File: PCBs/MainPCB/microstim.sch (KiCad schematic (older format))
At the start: 105 parts, among them J1 Conn_02x08_Odd_Even, J2 Conn_Coaxial, J3 Conn_Coaxial, J6 Screw_Terminal_01x02, J7 Conn_Coaxial, J8 Screw_Terminal_01x02, J9 Conn_Coaxial, SW1 SW_Push, U1 Teensy3.5, U10 AD8276, U11 INA826, U12 DG509ACWE, U13 CC3-0512DF-E, U14 ISO7760, U15 ISO7341C, U16 L78L05_SO8, U17 AD5752, U18 AD7321, U19 AD1582, U2 CC3-0512DF-E, U20 OPA197, U21 AD8276, U22 INA826, U23 DG509ACWE, U3 ISO7760, U4 ISO7341C, U5 L78L05_SO8, U6 AD5752, U7 AD7321, U8 AD1582, U9 OPA197

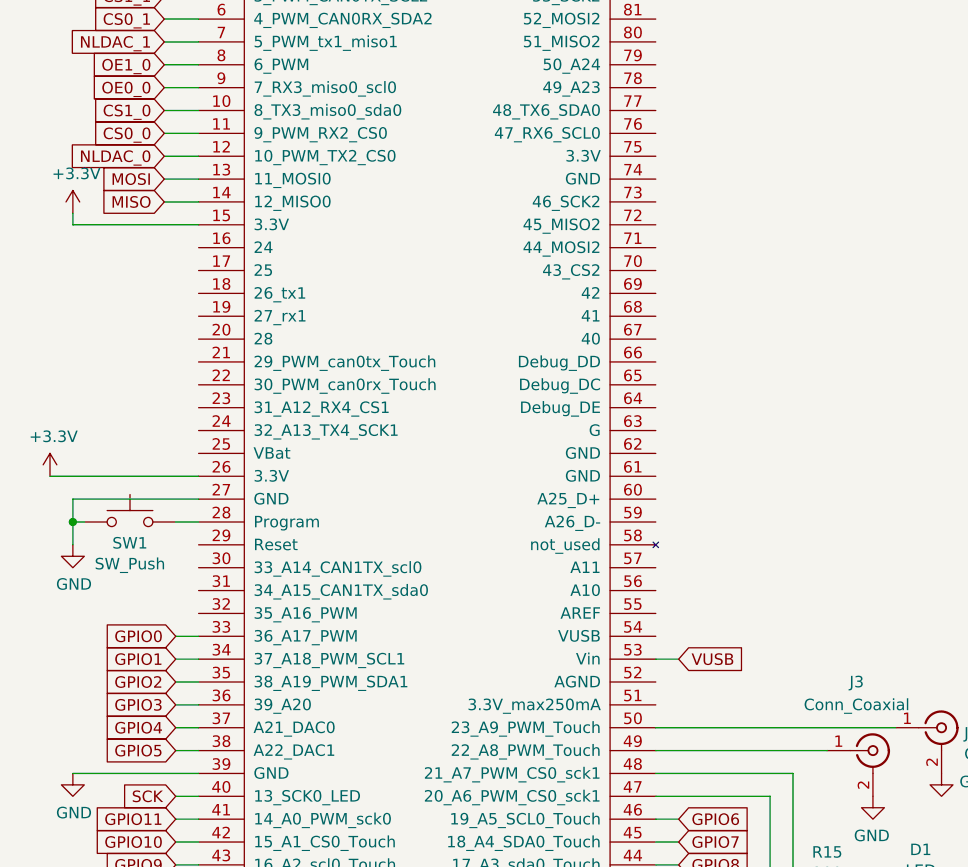
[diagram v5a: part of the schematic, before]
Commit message: merged in benchmarking into v3b. changed 3.3v power pin so that design is compatible with teensy 3.1/2 and 3.5/6.
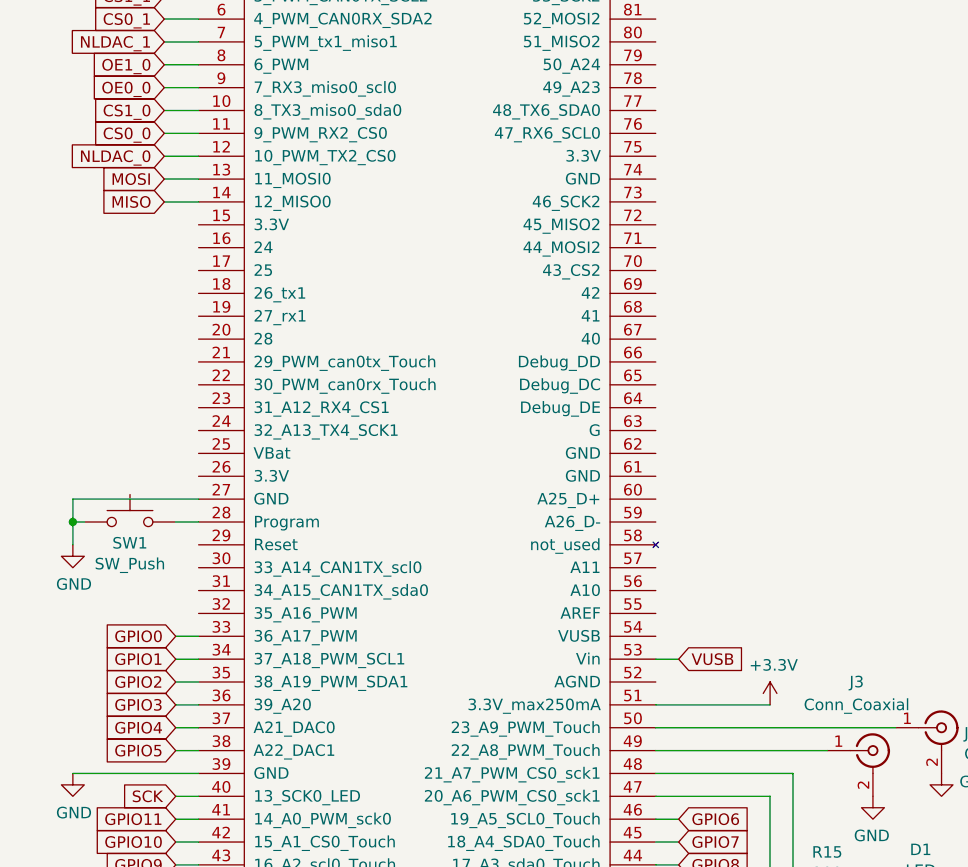
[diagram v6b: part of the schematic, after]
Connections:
- net +3V3: now also U1.51 (3.3V_max250mA); no longer U1.15 (3.3V), U1.26 (3.3V)
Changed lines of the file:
@@
 	6050 1850 5850 1850
 $Comp
-L power:+3.3V #PWR03
-U 1 1 5B7D2A4B
-P 700 1850
-F 0 "#PWR03" H 700 1700 50  0001 C CNN
-F 1 "+3.3V" H 715 2023 50  0000 C CNN
-F 2 "" H 700 1850 50  0001 C CNN
-F 3 "" H 700 1850 50  0001 C CNN
-	1    700  1850
-	1    0    0    -1
-$EndComp
-$Comp
 L Device:R_US R5
 U 1 1 5B7EBBC6
@@
 Text GLabel 1100 1500 0    50   Input ~ 0
 CS0_0
-Wire Wire Line
-	1250 1900 700  1900
-Wire Wire Line
-	700  1900 700  1850
 Text GLabel 8300 2450 0    50   Input ~ 0
 SCK_0i
@@
 Wire Wire Line
 	700  3200 700  3300
-Wire Wire Line
-	600  3000 1250 3000
 Text GLabel 2600 5200 2    50   Input ~ 0
 VUSB
@@
 Wire Wire Line
 	2600 5200 2500 5200
-$Comp
-L power:+3.3V #PWR0111
-U 1 1 5D1270A2
-P 600 3000
-F 0 "#PWR0111" H 600 2850 50  0001 C CNN
-F 1 "+3.3V" H 615 3173 50  0000 C CNN
-F 2 "" H 600 3000 50  0001 C CNN
-F 3 "" H 600 3000 50  0001 C CNN
-	1    600  3000
-	1    0    0    -1
-$EndComp
 Text GLabel 2600 5900 2    50   Input ~ 0
 GPIO11
@@
 Text Notes 5200 2700 1    79   ~ 0
 Stim channel 0
+$Comp
+L power:+3.3V #PWR0115
+U 1 1 5C672D77
+P 3750 4000
+F 0 "#PWR0115" H 3750 3850 50  0001 C CNN
+F 1 "+3.3V" H 3765 4173 50  0000 C CNN
+F 2 "" H 3750 4000 50  0001 C CNN
+F 3 "" H 3750 4000 50  0001 C CNN
+	1    3750 4000
+	1    0    0    -1
+$EndComp
+Wire Wire Line
+	3250 4000 3750 4000
 $EndSCHEMATC

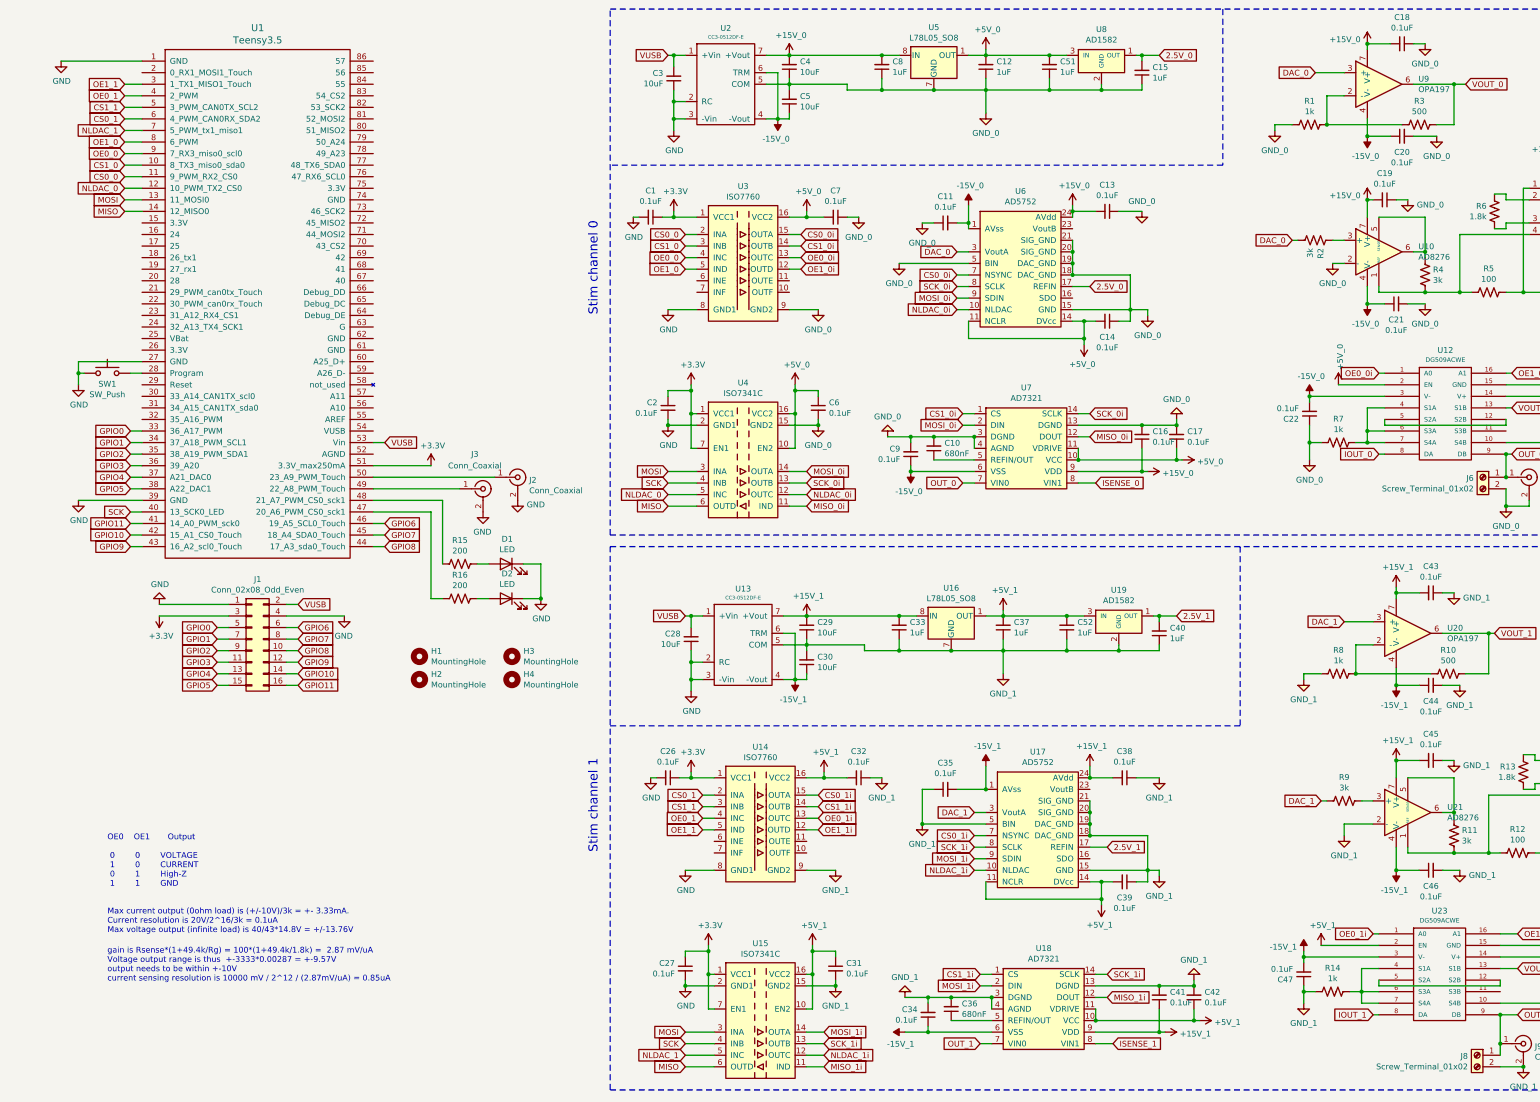
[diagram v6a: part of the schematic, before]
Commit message: boatload of updates via jons suggestions. de-isolated grounds via large resistors+capacitors (to prevent static buildup on animal or issues with large discharges). increased resistor values in voltage output non-inverting amplifier.
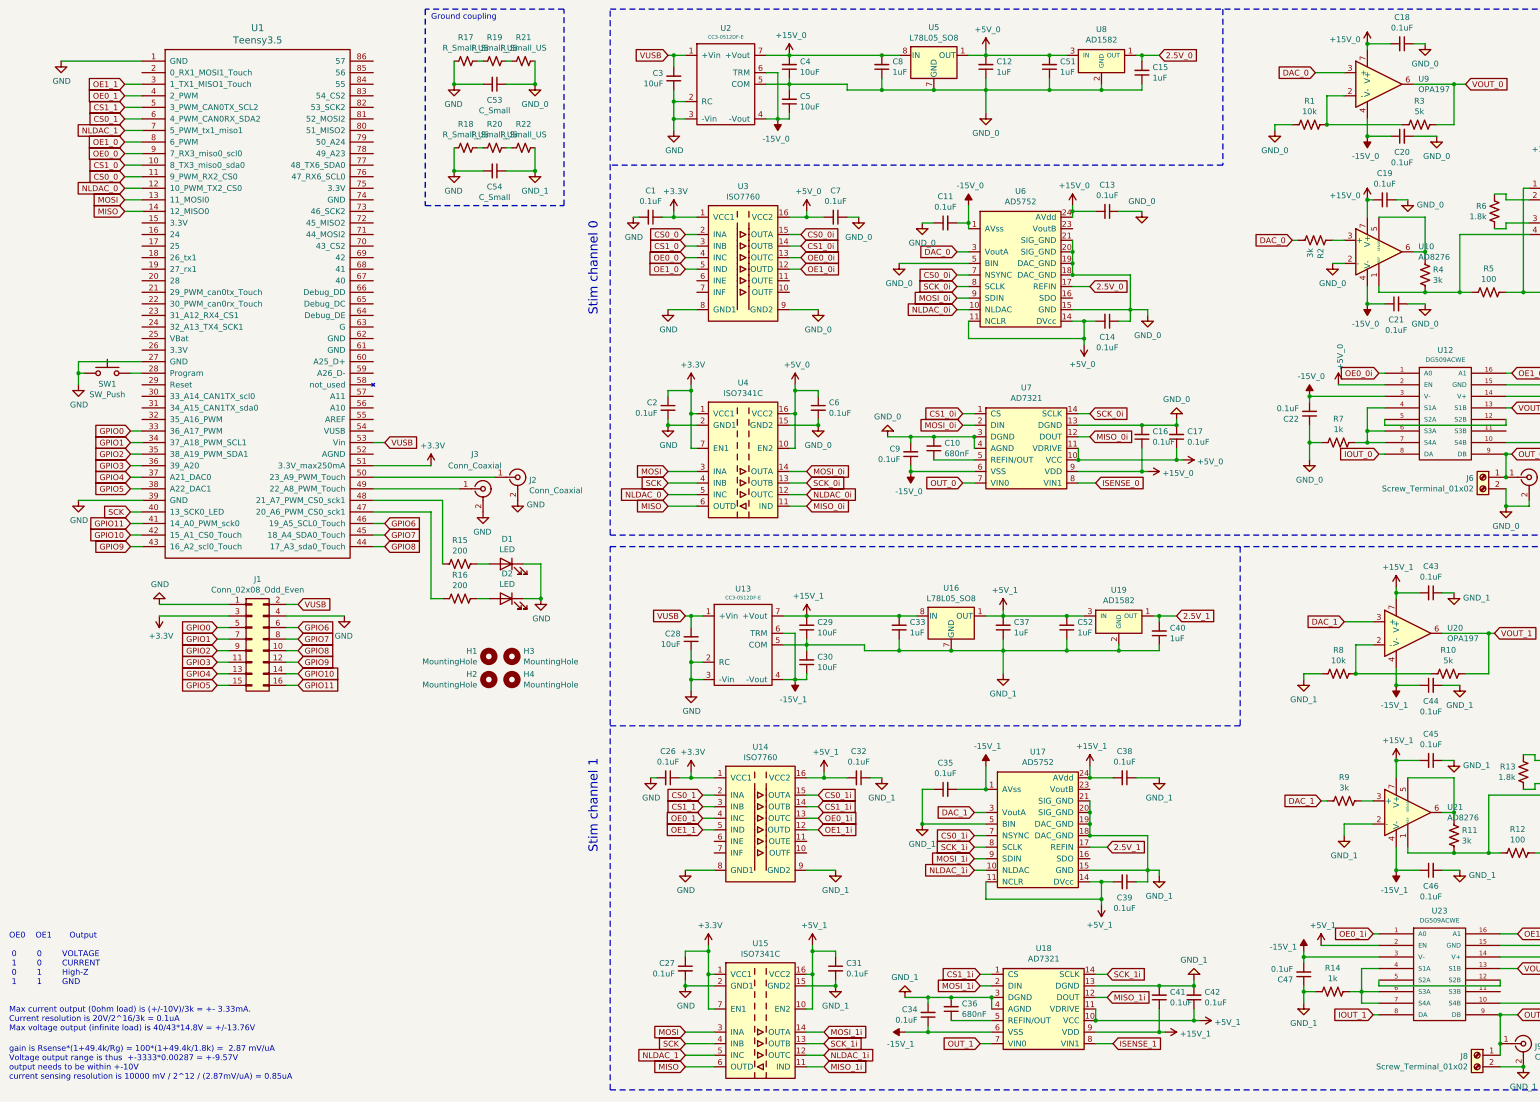
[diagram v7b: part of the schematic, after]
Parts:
- added C53, C54: C_Small, Capacitor_THT:C_Disc_D12.5mm_W5.0mm_P10.00mm, symbol Device:C_Small
- added R17, R18, R19, R20, R21, R22: R_Small_US, Resistor_SMD:R_1210_3225Metric_Pad1.42x2.65mm_HandSolder, symbol Device:R_Small_US
- R1, R8: value 1k -> 10k
- R10, R3: value 500 -> 5k
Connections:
- net GND: now also C53.2, C54.2, R17.2, R18.2
- net GND_0: now also C53.1, R21.1
- net GND_1: now also C54.1, R22.1
- new net: R17.1, R19.2
- new net: R19.1, R21.2
- new net: R18.1, R20.2
- new net: R20.1, R22.2
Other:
- note added: "Ground coupling"
- moved on the sheet: H1, H2
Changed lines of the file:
@@
 Wire Wire Line
 	13050 1700 13250 1700
-Text Notes 950  8550 0    50   ~ 0
+Text Notes 100  9400 0    50   ~ 0
 gain is Rsense*(1+49.4k/Rg) = 100*(1+49.4k/1.8k) =  2.87 mV/uA\nVoltage output range is thus  +-3333*0.00287 = +-9.57V\noutput needs to be within +-10V\ncurrent sensing resolution is 10000 mV / 2^12 / (2.87mV/uA) = 0.85uA\n\n
-Text Notes 950  8050 0    50   ~ 0
+Text Notes 100  8900 0    50   ~ 0
 Max current output (0ohm load) is (+/-10V)/3k = +- 3.33mA.\nCurrent resolution is 20V/2^16/3k = 0.1uA\nMax voltage output (infinite load) is 40/43*14.8V = +/-13.76V
 $Comp
@@
 L Mechanical:MountingHole H1
 U 1 1 5C07145A
-P 3650 5650
-F 0 "H1" H 3750 5696 50  0000 L CNN
-F 1 "MountingHole" H 3750 5605 50  0000 L CNN
-F 2 "MountingHole:MountingHole_4.3mm_M4" H 3650 5650 50  0001 C CNN
-F 3 "~" H 3650 5650 50  0001 C CNN
-	1    3650 5650
+P 4250 5650
+F 0 "H1" H 4150 5696 50  0000 R CNN
+F 1 "MountingHole" H 4150 5605 50  0000 R CNN
+F 2 "MountingHole:MountingHole_4.3mm_M4" H 4250 5650 50  0001 C CNN
+F 3 "~" H 4250 5650 50  0001 C CNN
+	1    4250 5650
 	1    0    0    -1
 $EndComp
@@
 L Mechanical:MountingHole H2
 U 1 1 5C071952
-P 3650 5850
-F 0 "H2" H 3750 5896 50  0000 L CNN
-F 1 "MountingHole" H 3750 5805 50  0000 L CNN
-F 2 "MountingHole:MountingHole_4.3mm_M4" H 3650 5850 50  0001 C CNN
-F 3 "~" H 3650 5850 50  0001 C CNN
-	1    3650 5850
+P 4250 5850
+F 0 "H2" H 4150 5896 50  0000 R CNN
+F 1 "MountingHole" H 4150 5805 50  0000 R CNN
+F 2 "MountingHole:MountingHole_4.3mm_M4" H 4250 5850 50  0001 C CNN
+F 3 "~" H 4250 5850 50  0001 C CNN
+	1    4250 5850
 	1    0    0    -1
 $EndComp
@@
 P 12300 1050
 F 0 "R3" V 12505 1050 50  0000 C CNN
-F 1 "500" V 12414 1050 50  0000 C CNN
+F 1 "5k" V 12414 1050 50  0000 C CNN
 F 2 "Resistor_SMD:R_0603_1608Metric" V 12340 1040 50  0001 C CNN
 F 3 "~" H 12300 1050 50  0001 C CNN
@@
 P 11350 1050
 F 0 "R1" V 11555 1050 50  0000 C CNN
-F 1 "1k" V 11464 1050 50  0000 C CNN
+F 1 "10k" V 11464 1050 50  0000 C CNN
 F 2 "Resistor_SMD:R_0603_1608Metric" V 11390 1040 50  0001 C CNN
 F 3 "~" H 11350 1050 50  0001 C CNN
@@
 P 12550 5800
 F 0 "R10" V 12755 5800 50  0000 C CNN
-F 1 "500" V 12664 5800 50  0000 C CNN
+F 1 "5k" V 12664 5800 50  0000 C CNN
 F 2 "Resistor_SMD:R_0603_1608Metric" V 12590 5790 50  0001 C CNN
 F 3 "~" H 12550 5800 50  0001 C CNN
@@
 P 11600 5800
 F 0 "R8" V 11805 5800 50  0000 C CNN
-F 1 "1k" V 11714 5800 50  0000 C CNN
+F 1 "10k" V 11714 5800 50  0000 C CNN
 F 2 "Resistor_SMD:R_0603_1608Metric" V 11640 5790 50  0001 C CNN
 F 3 "~" H 11600 5800 50  0001 C CNN
@@
 	13100 3900 13050 3900
 Connection ~ 13050 3900
-Text Notes 950  7650 0    50   ~ 0
+Text Notes 100  8500 0    50   ~ 0
 OE0    OE1       Output      \n\n 0        0        VOLTAGE     \n 1        0        CURRENT    \n 0        1        High-Z  \n 1        1        GND
 Wire Wire Line
@@
 Wire Wire Line
 	3250 4000 3750 4000
+$Comp
+L Device:R_Small_US R17
+U 1 1 5C780809
+P 4050 500
+F 0 "R17" V 3845 500 50  0000 C CNN
+F 1 "R_Small_US" V 3936 500 50  0000 C CNN
+F 2 "Resistor_SMD:R_1210_3225Metric_Pad1.42x2.65mm_HandSolder" H 4050 500 50  0001 C CNN
+F 3 "~" H 4050 500 50  0001 C CNN
+	1    4050 500
+	0    1    1    0
+$EndComp
+$Comp
+L Device:C_Small C53
+U 1 1 5C780E8F
+P 4300 700
+F 0 "C53" V 4437 700 50  0000 C CNN
+F 1 "C_Small" V 4528 700 50  0000 C CNN
+F 2 "Capacitor_THT:C_Disc_D12.5mm_W5.0mm_P10.00mm" H 4300 700 50  0001 C CNN
+F 3 "~" H 4300 700 50  0001 C CNN
+	1    4300 700
+	0    1    1    0
+$EndComp
+$Comp
+L Device:R_Small_US R19
+U 1 1 5C782E14
+P 4300 500
+F 0 "R19" V 4095 500 50  0000 C CNN
+F 1 "R_Small_US" V 4186 500 50  0000 C CNN
+F 2 "Resistor_SMD:R_1210_3225Metric_Pad1.42x2.65mm_HandSolder" H 4300 500 50  0001 C CNN
+F 3 "~" H 4300 500 50  0001 C CNN
+	1    4300 500
+	0    1    1    0
+$EndComp
+$Comp
+L Device:R_Small_US R21
+U 1 1 5C7DBF6D
+P 4550 500
+F 0 "R21" V 4345 500 50  0000 C CNN
+F 1 "R_Small_US" V 4436 500 50  0000 C CNN
+F 2 "Resistor_SMD:R_1210_3225Metric_Pad1.42x2.65mm_HandSolder" H 4550 500 50  0001 C CNN
+F 3 "~" H 4550 500 50  0001 C CNN
+	1    4550 500
+	0    1    1    0
+$EndComp
+Wire Wire Line
+	4400 500  4450 500
+Wire Wire Line
+	4150 500  4200 500
+Wire Wire Line
+	4200 700  3950 700
+Wire Wire Line
+	3950 700  3950 500
+Wire Wire Line
+	4400 700  4650 700
+Wire Wire Line
+	4650 700  4650 500
+$Comp
+L power:GND #PWR01
+U 1 1 5CA52EA1
+P 3950 700
+F 0 "#PWR01" H 3950 450 50  0001 C CNN
+F 1 "GND" H 3955 527 50  0000 C CNN
+F 2 "" H 3950 700 50  0001 C CNN
+F 3 "" H 3950 700 50  0001 C CNN
+	1    3950 700
+	-1   0    0    -1
+$EndComp
+Connection ~ 3950 700
+$Comp
+L natecermak:GND_0 #GND_035
+U 1 1 5CA52FF3
+P 4650 700
+F 0 "#GND_035" H 4650 490 50  0001 C CNN
+F 1 "GND_0" H 4650 527 50  0000 C CNN
+F 2 "" H 4500 350 50  0001 C CNN
+F 3 "" H 4500 350 50  0001 C CNN
+	1    4650 700
+	1    0    0    -1
+$EndComp
+Connection ~ 4650 700
+$Comp
+L Device:R_Small_US R18
+U 1 1 5CA53471
+P 4050 1250
+F 0 "R18" V 3845 1250 50  0000 C CNN
+F 1 "R_Small_US" V 3936 1250 50  0000 C CNN
+F 2 "Resistor_SMD:R_1210_3225Metric_Pad1.42x2.65mm_HandSolder" H 4050 1250 50  0001 C CNN
+F 3 "~" H 4050 1250 50  0001 C CNN
+	1    4050 1250
+	0    1    1    0
+$EndComp
+$Comp
+L Device:C_Small C54
+U 1 1 5CA53478
+P 4300 1450
+F 0 "C54" V 4437 1450 50  0000 C CNN
+F 1 "C_Small" V 4528 1450 50  0000 C CNN
+F 2 "Capacitor_THT:C_Disc_D12.5mm_W5.0mm_P10.00mm" H 4300 1450 50  0001 C CNN
+F 3 "~" H 4300 1450 50  0001 C CNN
+	1    4300 1450
+	0    1    1    0
+$EndComp
+$Comp
+L Device:R_Small_US R20
+U 1 1 5CA5347F
+P 4300 1250
+F 0 "R20" V 4095 1250 50  0000 C CNN
+F 1 "R_Small_US" V 4186 1250 50  0000 C CNN
+F 2 "Resistor_SMD:R_1210_3225Metric_Pad1.42x2.65mm_HandSolder" H 4300 1250 50  0001 C CNN
+F 3 "~" H 4300 1250 50  0001 C CNN
+	1    4300 1250
+	0    1    1    0
+$EndComp
+$Comp
+L Device:R_Small_US R22
+U 1 1 5CA53486
+P 4550 1250
+F 0 "R22" V 4345 1250 50  0000 C CNN
+F 1 "R_Small_US" V 4436 1250 50  0000 C CNN
+F 2 "Resistor_SMD:R_1210_3225Metric_Pad1.42x2.65mm_HandSolder" H 4550 1250 50  0001 C CNN
+F 3 "~" H 4550 1250 50  0001 C CNN
+	1    4550 1250
+	0    1    1    0
+$EndComp
+Wire Wire Line
+	4400 1250 4450 1250
+Wire Wire Line
+	4150 1250 4200 1250
+Wire Wire Line
+	4200 1450 3950 1450
+Wire Wire Line
+	3950 1450 3950 1250
+Wire Wire Line
+	4400 1450 4650 1450
+Wire Wire Line
+	4650 1450 4650 1250
+$Comp
+L power:GND #PWR03
+U 1 1 5CA53493
+P 3950 1450
+F 0 "#PWR03" H 3950 1200 50  0001 C CNN
+F 1 "GND" H 3955 1277 50  0000 C CNN
+F 2 "" H 3950 1450 50  0001 C CNN
+F 3 "" H 3950 1450 50  0001 C CNN
+	1    3950 1450
+	-1   0    0    -1
+$EndComp
+Connection ~ 3950 1450
+$Comp
+L natecermak:GND_1 #GND_036
+U 1 1 5CAB138B
+P 4650 1450
+F 0 "#GND_036" H 4650 1240 50  0001 C CNN
+F 1 "GND_1" H 4650 1277 50  0000 C CNN
+F 2 "" H 4500 1100 50  0001 C CNN
+F 3 "" H 4500 1100 50  0001 C CNN
+	1    4650 1450
+	1    0    0    -1
+$EndComp
+Connection ~ 4650 1450
+Wire Notes Line
+	3700 50   3700 1750
+Wire Notes Line
+	3700 1750 4900 1750
+Wire Notes Line
+	4900 1750 4900 50
+Wire Notes Line
+	4900 50   3700 50
+Text Notes 3750 150  0    50   ~ 0
+Ground coupling
 $EndSCHEMATC
